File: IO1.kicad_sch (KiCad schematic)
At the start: 17 parts, among them J801 SM06B-GHS-TB(LF)(SN), J802 SM04B-GHS-TB(LF)(SN), J803 SM04B-GHS-TB(LF)(SN), J804 SM04B-GHS-TB(LF)(SN), J805 SM06B-GHS-TB(LF)(SN)

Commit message: feat: add series resistor for PINIO
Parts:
- added R801, R802: 330, Resistor_SMD:R_0603_1608Metric_Pad0.98x0.95mm_HandSolder, symbol Device:R_Small
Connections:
- net D_PINIO0: now also R801.2; no longer J804.2 (Pin_2)
- net D_PINIO1: now also R802.2; no longer J804.3 (Pin_3)
- new net D_PINIO0R: J804.2 (Pin_2), R801.1
- new net D_PINIO1R: J804.3 (Pin_3), R802.1

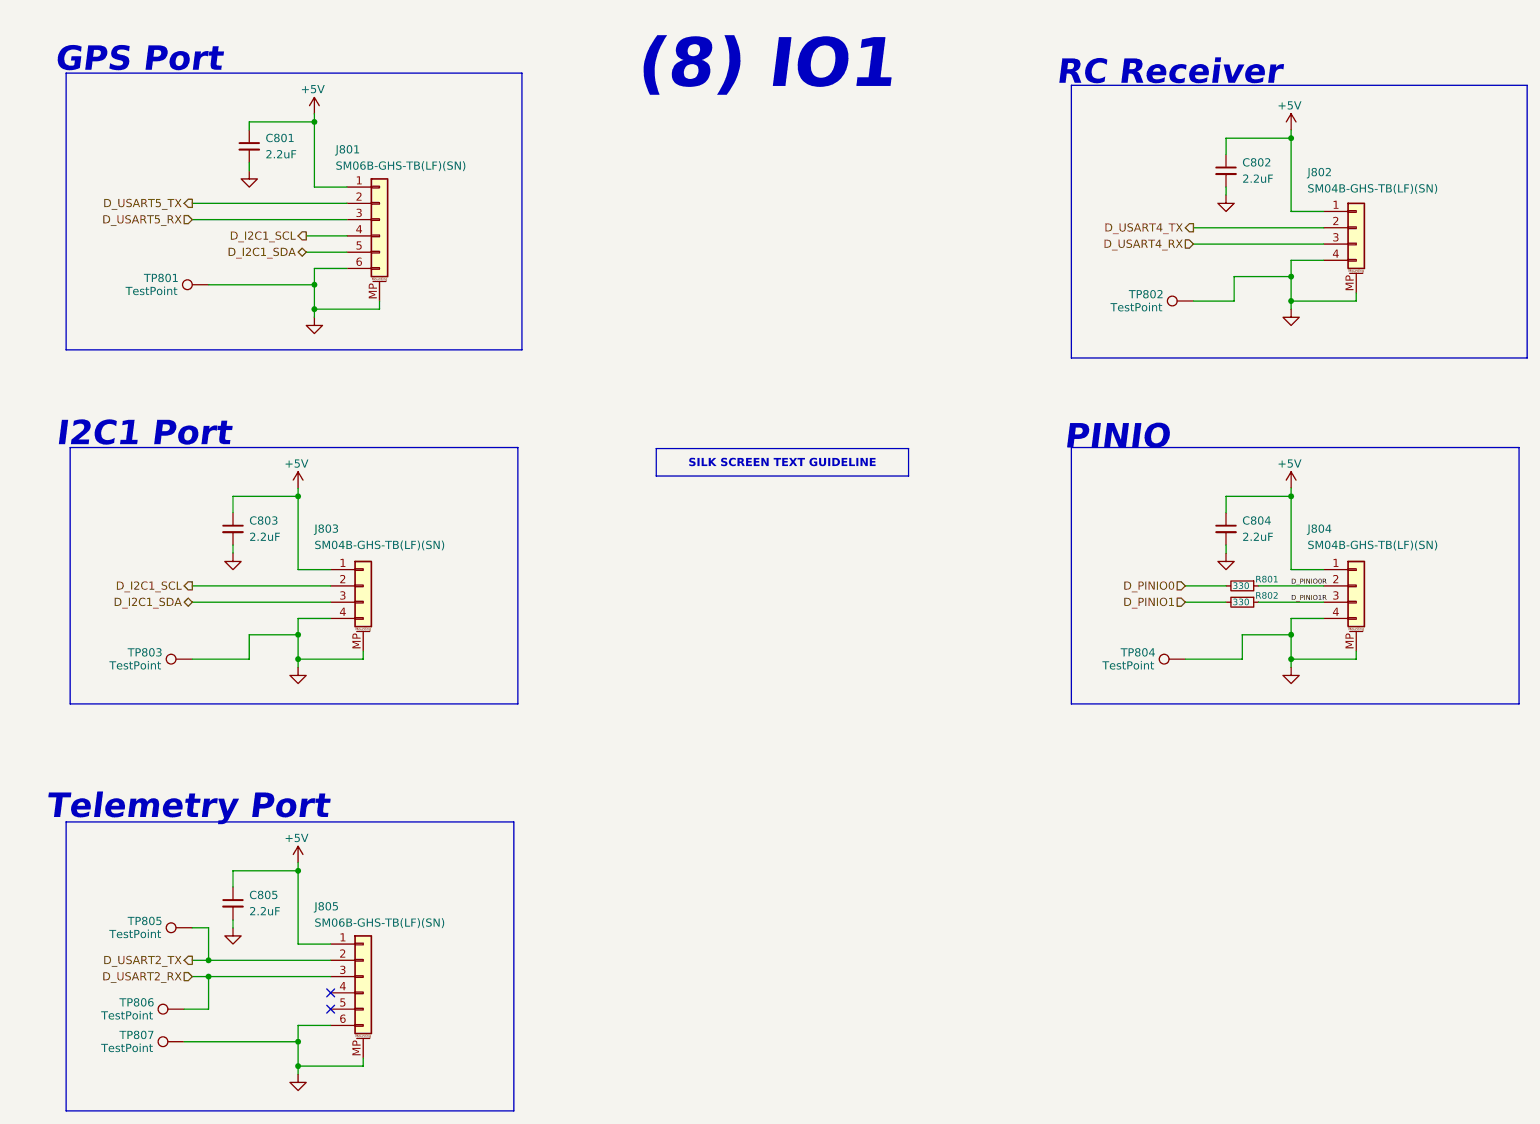
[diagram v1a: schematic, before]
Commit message: refactor: change tim5 ch 1 label to ch 2
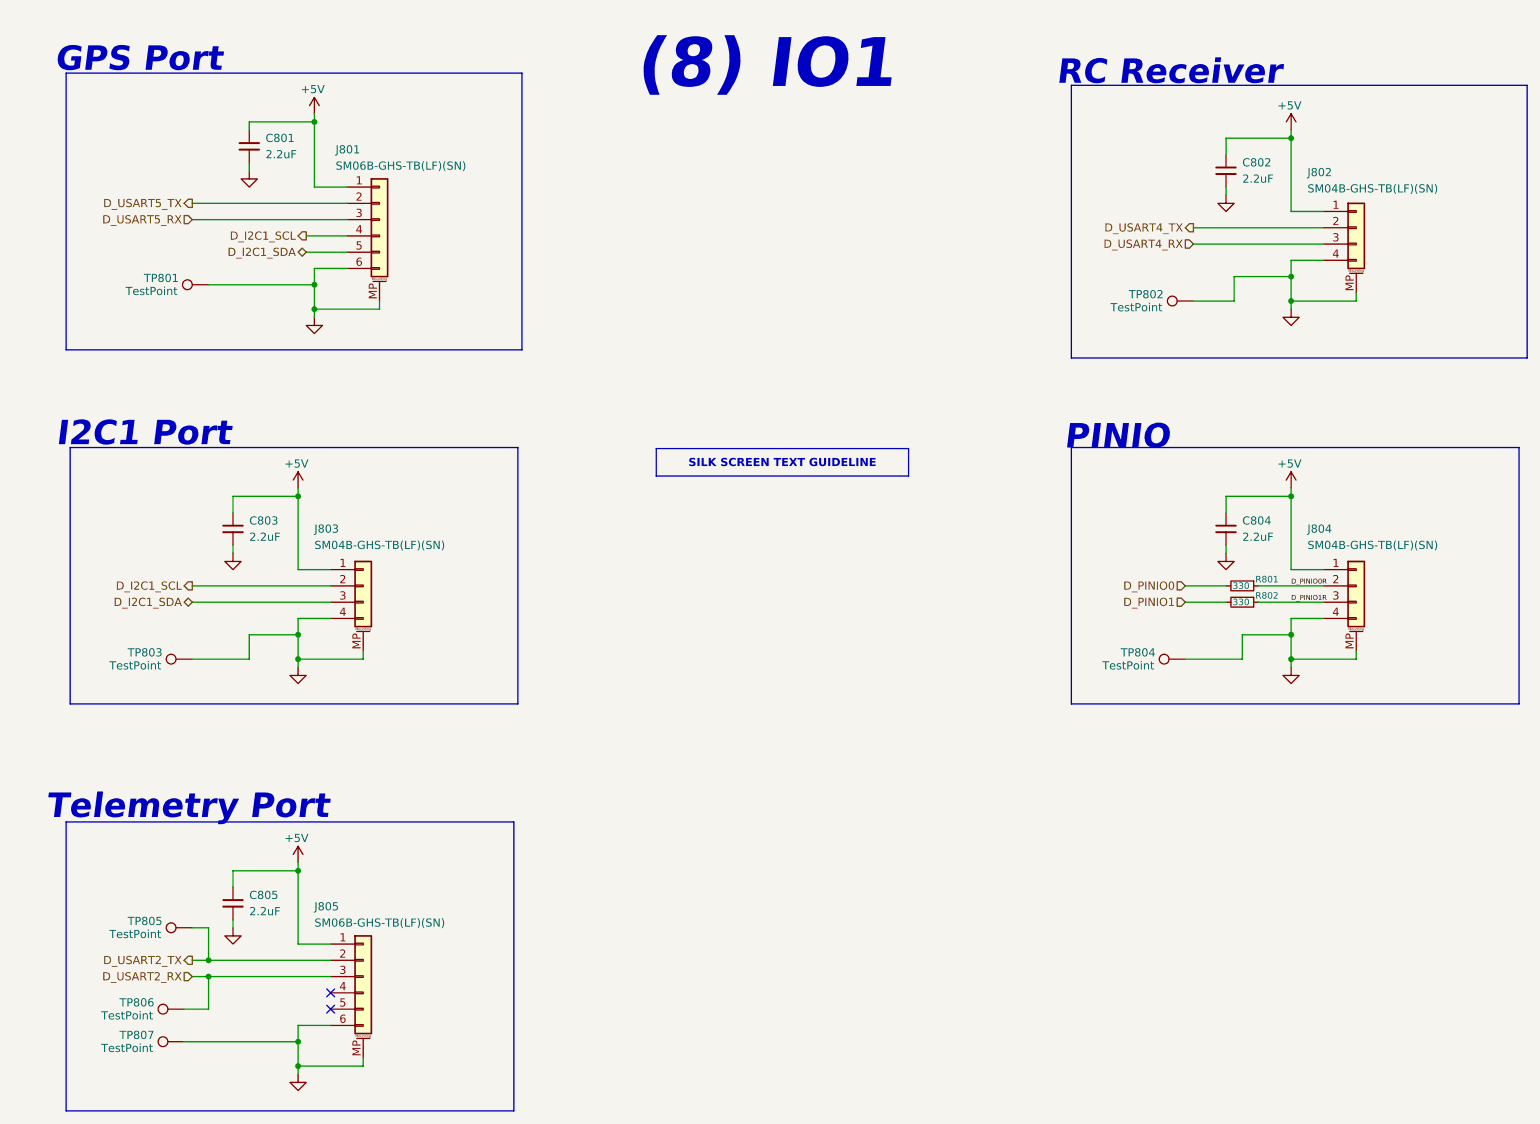
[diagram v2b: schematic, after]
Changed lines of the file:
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@@
 		(fields_autoplaced yes)
 		(property "Reference" "C803"
-			(at 60.96 96.5262 0)
+			(at 60.96 96.5199 0)
 			(show_name no)
 			(do_not_autoplace no)
@@
 		)
 		(property "Value" "2.2uF"
-			(at 60.96 99.0662 0)
+			(at 60.96 99.0599 0)
 			(show_name no)
 			(do_not_autoplace no)
@@
 			)
 		)
-		(property "Description" "Ceramic Capacitor, Ceramic, 16V, 20% +Tol, 20% -Tol, X7R, 15% TC, 2.2uF, Surface Mount, 0805"
-			(at 58.42 97.79 0)
+		(property "Description" "Unpolarized capacitor, small symbol"
+			(at 58.42 107.95 0)
 			(hide yes)
 			(show_name no)
@@
 		(fields_autoplaced yes)
 		(property "Reference" "C801"
-			(at 63.5 36.8362 0)
+			(at 63.5 36.8299 0)
 			(show_name no)
 			(do_not_autoplace no)
@@
 		)
 		(property "Value" "2.2uF"
-			(at 63.5 39.3762 0)
+			(at 63.5 39.3699 0)
 			(show_name no)
 			(do_not_autoplace no)
@@
 			)
 		)
-		(property "Description" "Ceramic Capacitor, Ceramic, 16V, 20% +Tol, 20% -Tol, X7R, 15% TC, 2.2uF, Surface Mount, 0805"
-			(at 60.96 38.1 0)
+		(property "Description" "Unpolarized capacitor, small symbol"
+			(at 60.96 48.26 0)
 			(hide yes)
 			(show_name no)
@@
 		(fields_autoplaced yes)
 		(property "Reference" "C805"
-			(at 60.96 154.9462 0)
+			(at 60.96 154.9399 0)
 			(show_name no)
 			(do_not_autoplace no)
@@
 		)
 		(property "Value" "2.2uF"
-			(at 60.96 157.4862 0)
+			(at 60.96 157.4799 0)
 			(show_name no)
 			(do_not_autoplace no)
@@
 			)
 		)
-		(property "Description" "Ceramic Capacitor, Ceramic, 16V, 20% +Tol, 20% -Tol, X7R, 15% TC, 2.2uF, Surface Mount, 0805"
-			(at 58.42 156.21 0)
+		(property "Description" "Unpolarized capacitor, small symbol"
+			(at 58.42 166.37 0)
 			(hide yes)
 			(show_name no)
@@
 		(fields_autoplaced yes)
 		(property "Reference" "C804"
-			(at 215.9 96.5262 0)
+			(at 215.9 96.5199 0)
 			(show_name no)
 			(do_not_autoplace no)
@@
 		)
 		(property "Value" "2.2uF"
-			(at 215.9 99.0662 0)
+			(at 215.9 99.0599 0)
 			(show_name no)
 			(do_not_autoplace no)
@@
 			)
 		)
-		(property "Description" "Ceramic Capacitor, Ceramic, 16V, 20% +Tol, 20% -Tol, X7R, 15% TC, 2.2uF, Surface Mount, 0805"
-			(at 213.36 97.79 0)
+		(property "Description" "Unpolarized capacitor, small symbol"
+			(at 213.36 107.95 0)
 			(hide yes)
 			(show_name no)
@@
 		(fields_autoplaced yes)
 		(property "Reference" "C802"
-			(at 215.9 40.6462 0)
+			(at 215.9 40.6399 0)
 			(show_name no)
 			(do_not_autoplace no)
@@
 		)
 		(property "Value" "2.2uF"
-			(at 215.9 43.1862 0)
+			(at 215.9 43.1799 0)
 			(show_name no)
 			(do_not_autoplace no)
@@
 			)
 		)
-		(property "Description" "Ceramic Capacitor, Ceramic, 16V, 20% +Tol, 20% -Tol, X7R, 15% TC, 2.2uF, Surface Mount, 0805"
-			(at 213.36 41.91 0)
-			(hide yes)
-			(show_name no)
+		(property "Description" "Unpolarized capacitor, small symbol"
+			(at 213.36 52.07 0)
+			(hide yes)
+			(show_name no)
